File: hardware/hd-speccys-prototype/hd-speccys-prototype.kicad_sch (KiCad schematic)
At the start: 20 parts, among them J1 PI_ZERO_2x20, J3 ULA_SOCKET_02x20, J4 Conn_01x03_Pin, J5 POWER 9-20VDC, U1 74LS30, U4 TSR_1-2450, U5 74HC244, U6 74HC244

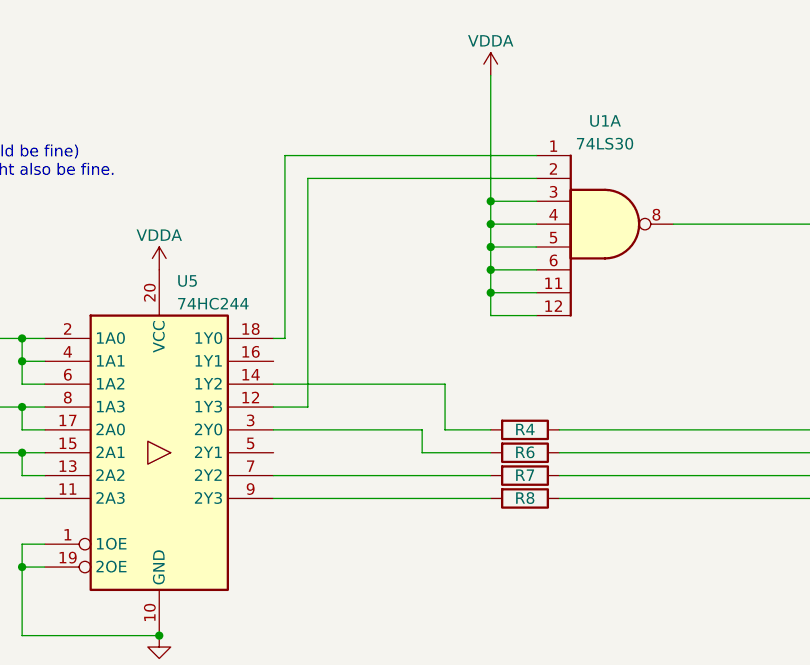
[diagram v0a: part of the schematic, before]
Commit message: refactor: moved screen processing code to zxscreen so don't need a separate buffer and copy.
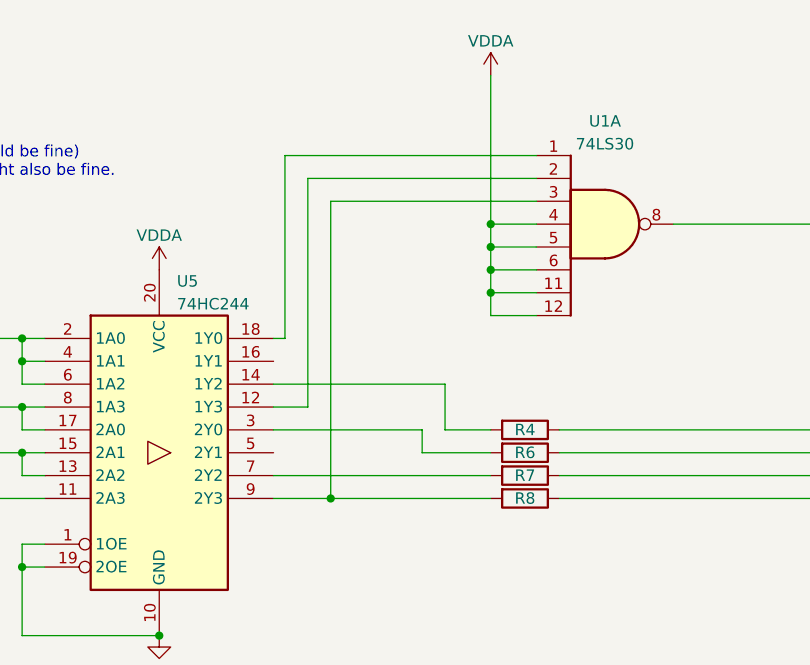
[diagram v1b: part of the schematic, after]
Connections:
- net VDDA: no longer U1.3
- net at R8.2, U5.9 (2Y3): now also U1.3
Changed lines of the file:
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@@
   (junction (at 255.27 120.65) (diameter 0) (color 0 0 0 0)
   )
+  (junction (at 144.78 40.64) (diameter 0) (color 0 0 0 0)
+  )
   (junction (at 255.27 80.01) (diameter 0) (color 0 0 0 0)
   )
@@
   (junction (at 255.27 107.95) (diameter 0) (color 0 0 0 0)
   )
+  (junction (at 127 71.12) (diameter 0) (color 0 0 0 0)
+  )
   (junction (at 144.78 45.72) (diameter 0) (color 0 0 0 0)
   )
-  (junction (at 144.78 38.1) (diameter 0) (color 0 0 0 0)
-  )
   (junction (at 255.27 67.31) (diameter 0) (color 0 0 0 0)
   )
-  (junction (at 144.78 40.64) (diameter 0) (color 0 0 0 0)
-  )
   (junction (at 92.71 53.34) (diameter 0) (color 0 0 0 0)
   )
@@
     (stroke (width 0) (type default))
   )
-  (wire (pts (xy 144.78 38.1) (xy 149.86 38.1))
+  (wire (pts (xy 127 38.1) (xy 149.86 38.1))
     (stroke (width 0) (type default))
   )
@@
     (stroke (width 0) (type default))
   )
-  (wire (pts (xy 120.65 71.12) (xy 144.78 71.12))
+  (wire (pts (xy 120.65 71.12) (xy 127 71.12))
     (stroke (width 0) (type default))
   )
@@
     (stroke (width 0) (type default))
   )
+  (wire (pts (xy 144.78 24.13) (xy 144.78 40.64))
+    (stroke (width 0) (type default))
+  )
   (wire (pts (xy 95.25 119.38) (xy 72.39 119.38))
     (stroke (width 0) (type default))
@@
     (stroke (width 0) (type default))
   )
+  (wire (pts (xy 127 71.12) (xy 144.78 71.12))
+    (stroke (width 0) (type default))
+  )
   (wire (pts (xy 120.65 119.38) (xy 144.78 119.38))
     (stroke (width 0) (type default))
@@
     (stroke (width 0) (type default))
   )
-  (wire (pts (xy 144.78 24.13) (xy 144.78 38.1))
-    (stroke (width 0) (type default))
-  )
   (wire (pts (xy 137.16 63.5) (xy 137.16 66.04))
     (stroke (width 0) (type default))
@@
     (stroke (width 0) (type default))
   )
+  (wire (pts (xy 127 38.1) (xy 127 71.12))
+    (stroke (width 0) (type default))
+  )
   (wire (pts (xy 124.46 35.56) (xy 124.46 60.96))
     (stroke (width 0) (type default))
@@
     (stroke (width 0) (type default))
   )
-  (wire (pts (xy 144.78 38.1) (xy 144.78 40.64))
-    (stroke (width 0) (type default))
-  )
